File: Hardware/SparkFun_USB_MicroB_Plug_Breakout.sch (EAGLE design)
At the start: 3 parts

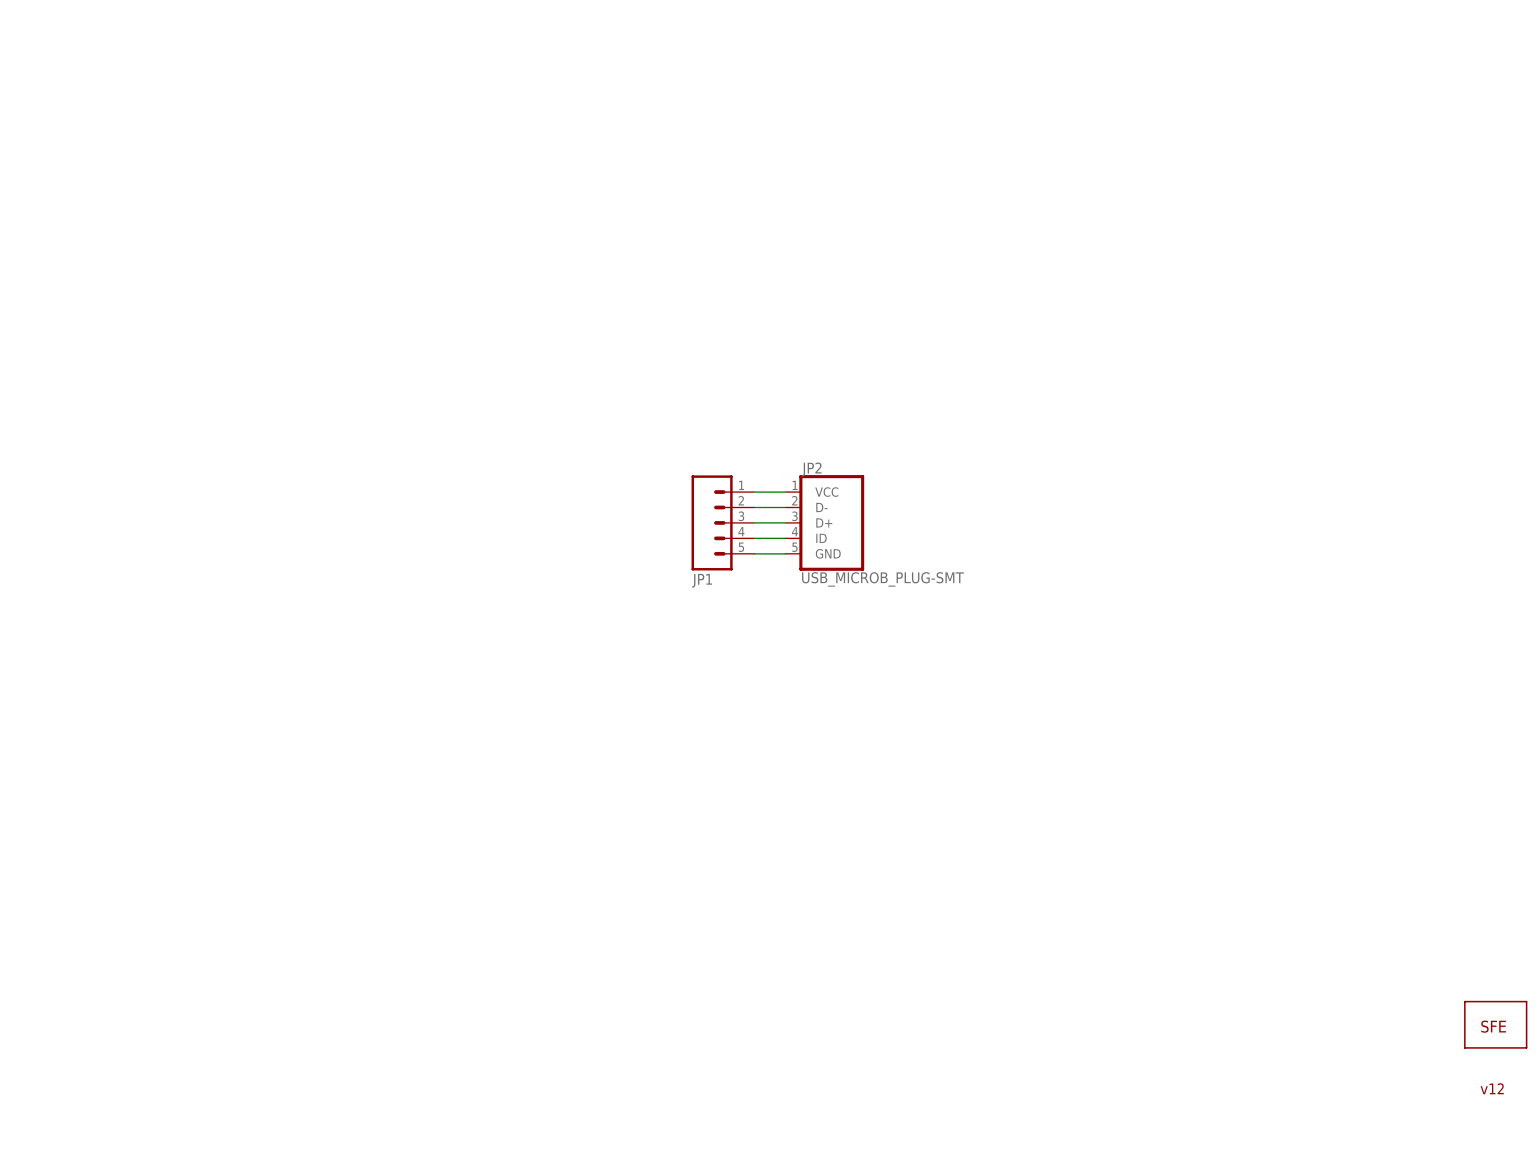
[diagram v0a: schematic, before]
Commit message: Fixed USB Micro footprint.  Added OSHW SPK logo
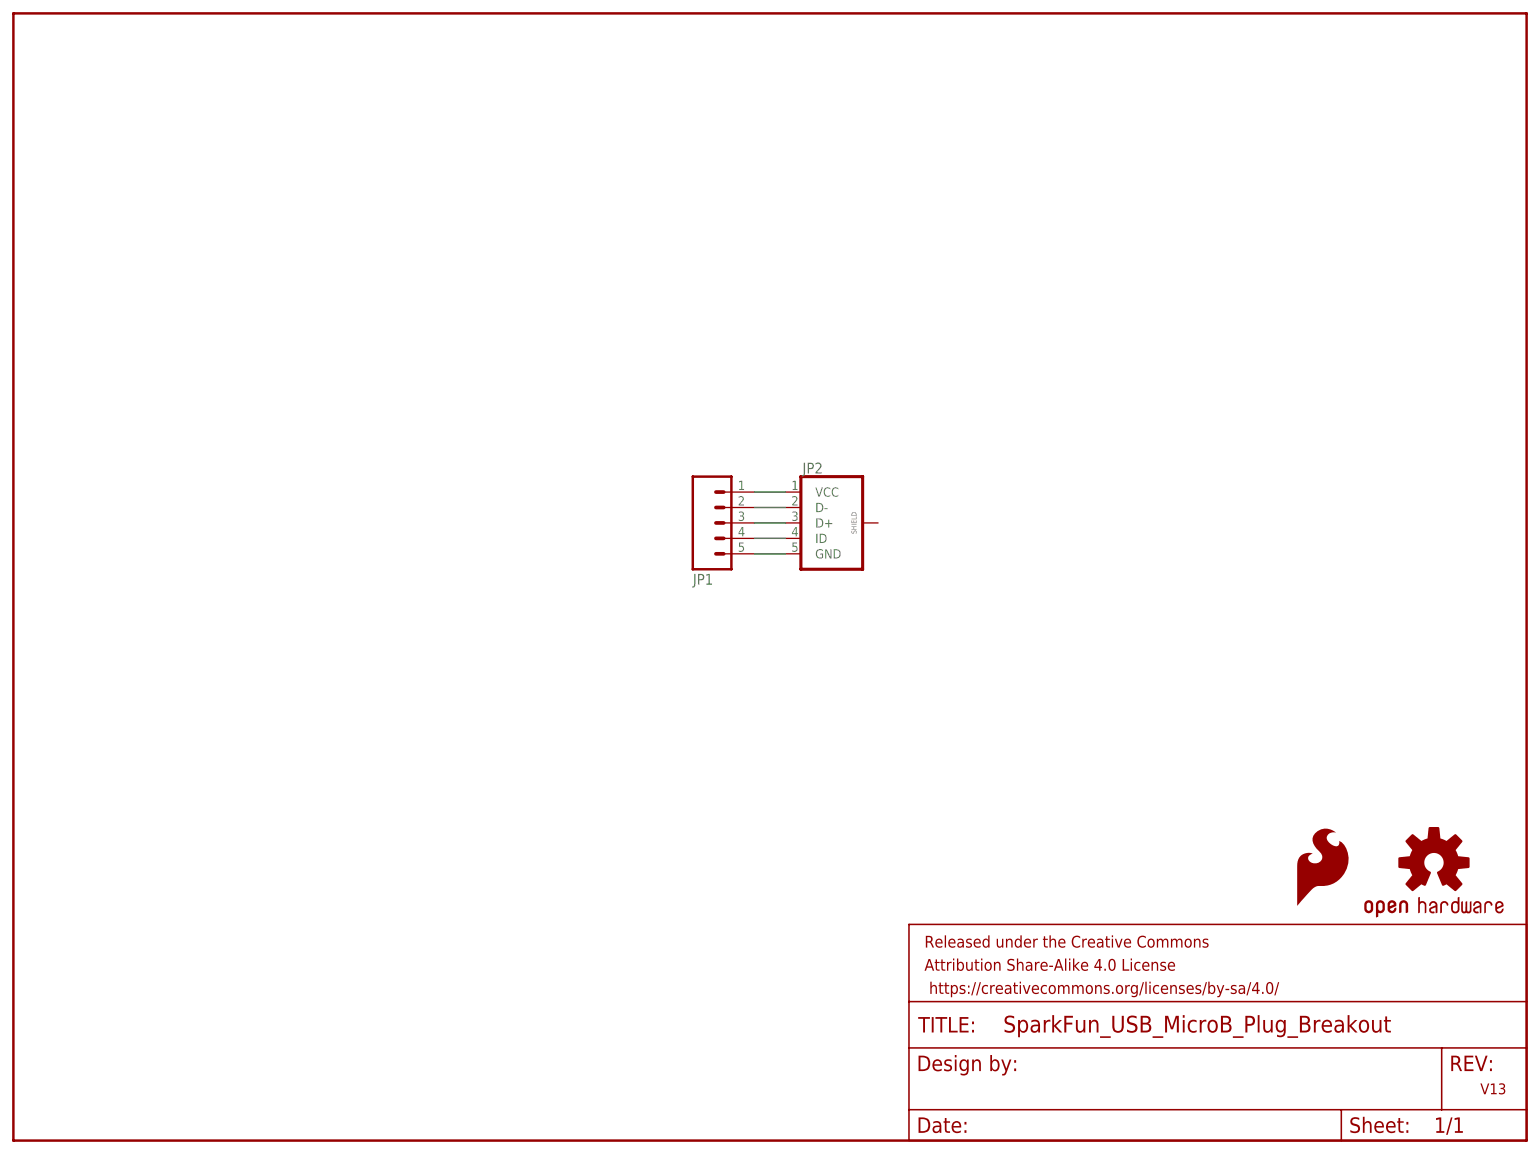
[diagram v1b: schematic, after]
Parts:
- removed JP3: LOGO-SFESK, SparkFun:LOGO-SFESK
- added FRAME1: FRAME-LETTER, SparkFun-Aesthetics:FRAME-LETTER
- added LOGO1: OSHW-LOGOS, SparkFun-Aesthetics:OSHW-LOGOS
- added LOGO2: SFE_LOGO_FLAME.1_INCH, SparkFun-Aesthetics:SFE_LOGO_FLAME.1_INCH
- JP2: value USB_MICROB_PLUG-SMT -> (none); device SparkFun:USB_MICROB_PLUG-SMT -> SparkFun-Connectors:USB_MICROB_PLUG-SMT
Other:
- note added: "V13"
- note removed: "v12"
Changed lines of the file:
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@@
 <?xml version="1.0" encoding="utf-8"?>
 <!DOCTYPE eagle SYSTEM "eagle.dtd">
-<eagle version="7.2.0">
+<eagle version="7.1.0">
 <drawing>
 <settings>
@@
 <layer number="54" name="bGND_GNDA" color="1" fill="9" visible="no" active="no"/>
 <layer number="56" name="wert" color="7" fill="1" visible="no" active="no"/>
+<layer number="57" name="tCAD" color="7" fill="1" visible="no" active="no"/>
+<layer number="59" name="tCarbon" color="7" fill="1" visible="no" active="no"/>
+<layer number="60" name="bCarbon" color="7" fill="1" visible="no" active="no"/>
+<layer number="90" name="Modules" color="5" fill="1" visible="yes" active="yes"/>
 <layer number="91" name="Nets" color="2" fill="1" visible="yes" active="yes"/>
 <layer number="92" name="Busses" color="1" fill="1" visible="yes" active="yes"/>
@@
 <layer number="97" name="Info" color="7" fill="1" visible="yes" active="yes"/>
 <layer number="98" name="Guide" color="6" fill="1" visible="yes" active="yes"/>
+<layer number="99" name="SpiceOrder" color="7" fill="1" visible="yes" active="yes"/>
 <layer number="100" name="Muster" color="7" fill="1" visible="no" active="no"/>
 <layer number="101" name="Patch_Top" color="12" fill="4" visible="yes" active="yes"/>
@@
 <layer number="106" name="bPlate" color="7" fill="1" visible="yes" active="yes"/>
 <layer number="107" name="Crop" color="7" fill="1" visible="yes" active="yes"/>
+<layer number="108" name="tplace-old" color="10" fill="1" visible="no" active="yes"/>
+<layer number="109" name="ref-old" color="11" fill="1" visible="no" active="yes"/>
+<layer number="110" name="fp0" color="7" fill="1" visible="no" active="yes"/>
+<layer number="111" name="LPC17xx" color="7" fill="1" visible="no" active="yes"/>
+<layer number="112" name="tSilk" color="7" fill="1" visible="no" active="yes"/>
+<layer number="113" name="IDFDebug" color="4" fill="1" visible="no" active="yes"/>
 <layer number="116" name="Patch_BOT" color="9" fill="4" visible="yes" active="yes"/>
 <layer number="121" name="_tsilk" color="7" fill="1" visible="yes" active="yes"/>
 <layer number="122" name="_bsilk" color="7" fill="1" visible="yes" active="yes"/>
+<layer number="123" name="tTestmark" color="7" fill="1" visible="no" active="yes"/>
+<layer number="124" name="bTestmark" color="7" fill="1" visible="no" active="yes"/>
+<layer number="125" name="_tNames" color="7" fill="1" visible="no" active="yes"/>
+<layer number="126" name="_bNames" color="7" fill="1" visible="no" active="yes"/>
+<layer number="127" name="_tValues" color="7" fill="1" visible="no" active="yes"/>
+<layer number="128" name="_bValues" color="7" fill="1" visible="no" active="yes"/>
+<layer number="129" name="Mask" color="7" fill="1" visible="yes" active="yes"/>
+<layer number="131" name="tAdjust" color="7" fill="1" visible="no" active="yes"/>
+<layer number="132" name="bAdjust" color="7" fill="1" visible="no" active="yes"/>
+<layer number="144" name="Drill_legend" color="7" fill="1" visible="no" active="yes"/>
+<layer number="150" name="Notes" color="7" fill="1" visible="no" active="yes"/>
 <layer number="151" name="HeatSink" color="7" fill="1" visible="yes" active="yes"/>
+<layer number="152" name="_bDocu" color="7" fill="1" visible="no" active="yes"/>
+<layer number="153" name="FabDoc1" color="7" fill="1" visible="no" active="yes"/>
+<layer number="154" name="FabDoc2" color="7" fill="1" visible="no" active="yes"/>
+<layer number="155" name="FabDoc3" color="7" fill="1" visible="no" active="yes"/>
+<layer number="199" name="Contour" color="7" fill="1" visible="no" active="yes"/>
 <layer number="200" name="200bmp" color="1" fill="10" visible="yes" active="yes"/>
 <layer number="201" name="201bmp" color="2" fill="10" visible="yes" active="yes"/>
@@
 <layer number="207" name="207bmp" color="8" fill="10" visible="yes" active="yes"/>
 <layer number="208" name="208bmp" color="9" fill="10" visible="yes" active="yes"/>
+<layer number="209" name="209bmp" color="7" fill="1" visible="no" active="yes"/>
+<layer number="210" name="210bmp" color="7" fill="1" visible="no" active="yes"/>
+<layer number="211" name="211bmp" color="7" fill="1" visible="no" active="yes"/>
+<layer number="212" name="212bmp" color="7" fill="1" visible="no" active="yes"/>
+<layer number="213" name="213bmp" color="7" fill="1" visible="no" active="yes"/>
+<layer number="214" name="214bmp" color="7" fill="1" visible="no" active="yes"/>
+<layer number="215" name="215bmp" color="7" fill="1" visible="no" active="yes"/>
+<layer number="216" name="216bmp" color="7" fill="1" visible="no" active="yes"/>
+<layer number="217" name="217bmp" color="18" fill="1" visible="no" active="no"/>
+<layer number="218" name="218bmp" color="19" fill="1" visible="no" active="no"/>
+<layer number="219" name="219bmp" color="20" fill="1" visible="no" active="no"/>
+<layer number="220" name="220bmp" color="21" fill="1" visible="no" active="no"/>
+<layer number="221" name="221bmp" color="22" fill="1" visible="no" active="no"/>
+<layer number="222" name="222bmp" color="23" fill="1" visible="no" active="no"/>
+<layer number="223" name="223bmp" color="24" fill="1" visible="no" active="no"/>
+<layer number="224" name="224bmp" color="25" fill="1" visible="no" active="no"/>
+<layer number="225" name="225bmp" color="7" fill="1" visible="yes" active="yes"/>
+<layer number="226" name="226bmp" color="7" fill="1" visible="yes" active="yes"/>
+<layer number="227" name="227bmp" color="7" fill="1" visible="yes" active="yes"/>
+<layer number="228" name="228bmp" color="7" fill="1" visible="yes" active="yes"/>
+<layer number="229" name="229bmp" color="7" fill="1" visible="yes" active="yes"/>
+<layer number="230" name="230bmp" color="7" fill="1" visible="yes" active="yes"/>
+<layer number="231" name="231bmp" color="7" fill="1" visible="yes" active="yes"/>
+<layer number="248" name="Housing" color="7" fill="1" visible="no" active="yes"/>
+<layer number="249" name="Edge" color="7" fill="1" visible="no" active="yes"/>
 <layer number="250" name="Descript" color="3" fill="1" visible="no" active="no"/>
 <layer number="251" name="SMDround" color="12" fill="11" visible="no" active="no"/>
 <layer number="254" name="cooling" color="7" fill="1" visible="yes" active="yes"/>
+<layer number="255" name="routoute" color="7" fill="1" visible="yes" active="yes"/>
 </layers>
-<schematic xreflabel="%F%N/%S" xrefpart="/%S">
+<schematic xreflabel="%F%N/%S" xrefpart="/%S.%C%R">
 <attributes>
 </attributes>
@@
 </classes>
 <parts>
-<part name="FRAME1" library="SparkFun" deviceset="FRAME-LETTER" device=""/>
+<part name="FRAME1" library="SparkFun-Aesthetics" deviceset="FRAME-LETTER" device=""/>
 <part name="JP1" library="SparkFun" deviceset="M05" device="PTH"/>
-<part name="JP3" library="SparkFun" deviceset="LOGO-SFE" device="SK"/>
-<part name="JP2" library="SparkFun" deviceset="USB_MICROB_PLUG" device="-SMT"/>
+<part name="JP2" library="SparkFun-Connectors" deviceset="USB_MICROB_PLUG" device="-SMT"/>
+<part name="LOGO1" library="SparkFun-Aesthetics" deviceset="OSHW-LOGO" device="S"/>
+<part name="LOGO2" library="SparkFun-Aesthetics" deviceset="SFE_LOGO_FLAME" device=".1_INCH"/>
 </parts>
 <sheets>
 <sheet>
 <plain>
-<text x="241.3" y="7.62" size="1.778" layer="94">v12</text>
+<text x="241.3" y="7.62" size="1.778" layer="94">V13</text>
 </plain>
 <instances>
 <instance part="FRAME1" gate="G$1" x="0" y="0"/>
-<instance part="FRAME1" gate="G$2" x="147.32" y="0"/>
+<instance part="FRAME1" gate="V" x="147.32" y="0"/>
 <instance part="JP1" gate="G$1" x="114.3" y="101.6" rot="MR180"/>
-<instance part="JP3" gate="G$1" x="241.3" y="17.78"/>
 <instance part="JP2" gate="G$1" x="134.62" y="101.6"/>
+<instance part="LOGO1" gate="G$1" x="233.68" y="45.72"/>
+<instance part="LOGO2" gate="G$1" x="210.82" y="38.1"/>
 </instances>
 <busses>

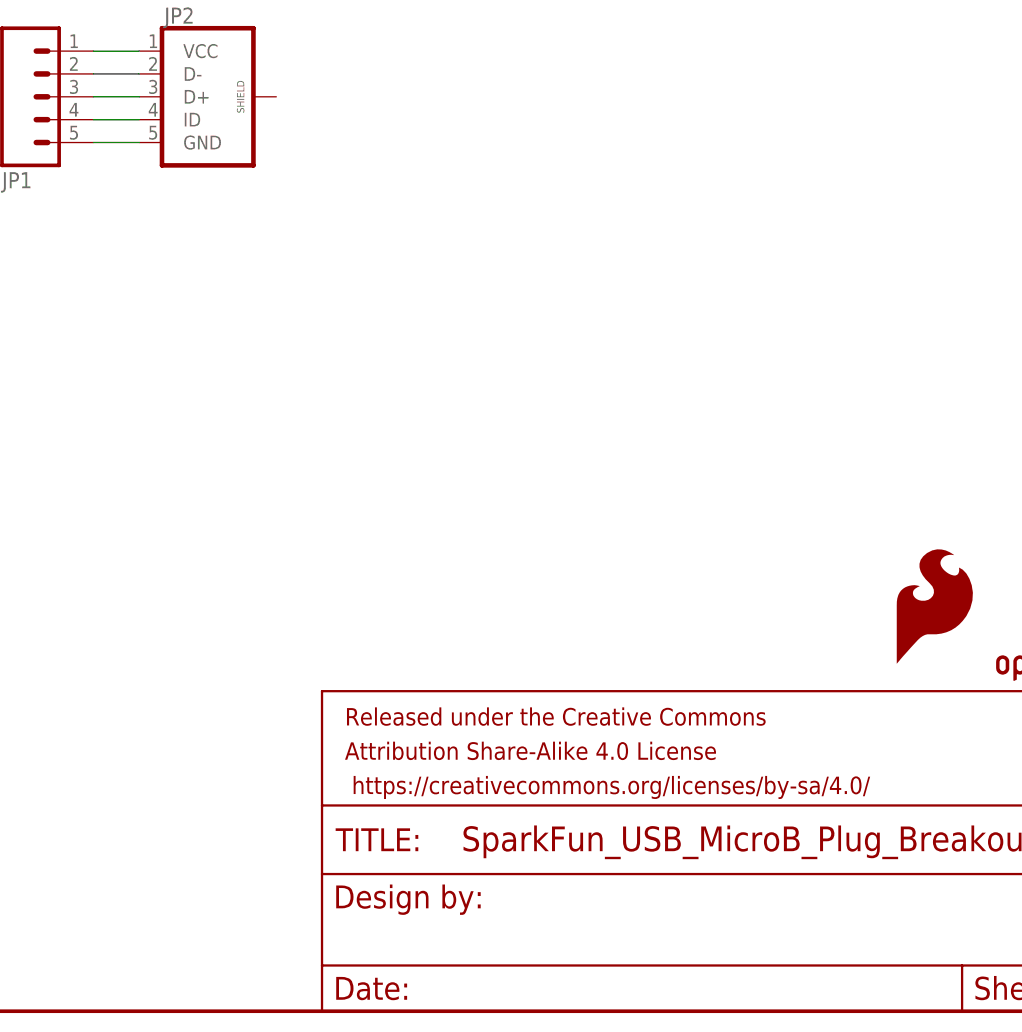
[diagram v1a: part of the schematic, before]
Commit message: Added silk and prod attributes.
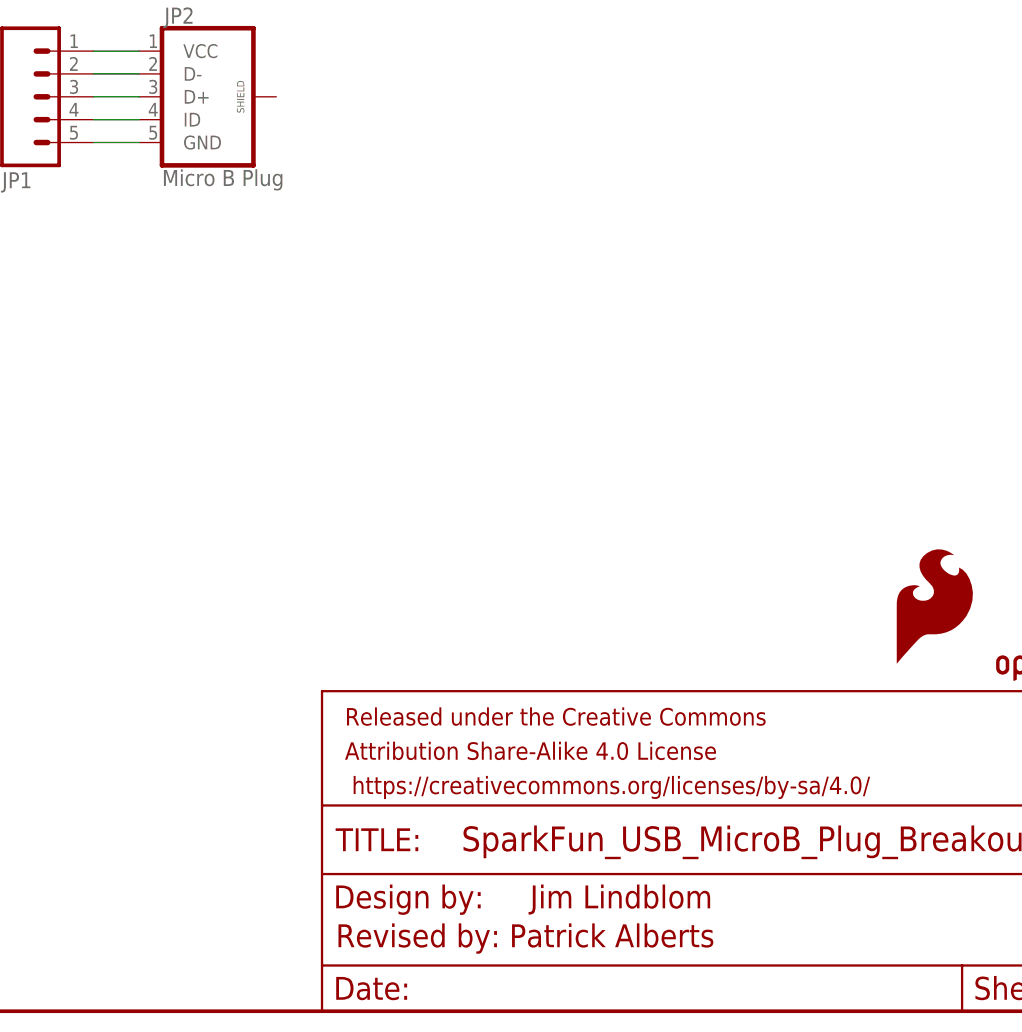
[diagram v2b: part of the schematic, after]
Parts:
- JP2: value (none) -> Micro B Plug
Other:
- note added: "Jim Lindblom"
- note added: "Revised by: Patrick Alberts"
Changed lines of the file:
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@@
 <part name="FRAME1" library="SparkFun-Aesthetics" deviceset="FRAME-LETTER" device=""/>
 <part name="JP1" library="SparkFun" deviceset="M05" device="PTH"/>
-<part name="JP2" library="SparkFun-Connectors" deviceset="USB_MICROB_PLUG" device="-SMT"/>
+<part name="JP2" library="SparkFun-Connectors" deviceset="USB_MICROB_PLUG" device="-SMT" value="Micro B Plug"/>
 <part name="LOGO1" library="SparkFun-Aesthetics" deviceset="OSHW-LOGO" device="S"/>
 <part name="LOGO2" library="SparkFun-Aesthetics" deviceset="SFE_LOGO_FLAME" device=".1_INCH"/>
@@
 <plain>
 <text x="241.3" y="7.62" size="1.778" layer="94">V13</text>
+<text x="148.844" y="7.112" size="2.54" layer="94">Revised by: Patrick Alberts</text>
+<text x="170.434" y="11.43" size="2.54" layer="94">Jim Lindblom</text>
 </plain>
 <instances>

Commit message: Added Measures.
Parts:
- JP2: value Micro B Plug -> USB Micro B Plug
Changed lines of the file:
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@@
 <?xml version="1.0" encoding="utf-8"?>
 <!DOCTYPE eagle SYSTEM "eagle.dtd">
-<eagle version="7.1.0">
+<eagle version="6.4">
 <drawing>
 <settings>
@@
 <part name="FRAME1" library="SparkFun-Aesthetics" deviceset="FRAME-LETTER" device=""/>
 <part name="JP1" library="SparkFun" deviceset="M05" device="PTH"/>
-<part name="JP2" library="SparkFun-Connectors" deviceset="USB_MICROB_PLUG" device="-SMT" value="Micro B Plug"/>
+<part name="JP2" library="SparkFun-Connectors" deviceset="USB_MICROB_PLUG" device="-SMT" value="USB Micro B Plug"/>
 <part name="LOGO1" library="SparkFun-Aesthetics" deviceset="OSHW-LOGO" device="S"/>
 <part name="LOGO2" library="SparkFun-Aesthetics" deviceset="SFE_LOGO_FLAME" device=".1_INCH"/>
